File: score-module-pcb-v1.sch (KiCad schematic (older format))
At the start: 2 parts, among them P1 PINBALL-CONNECTOR, P2 PINBALL-CONNECTOR

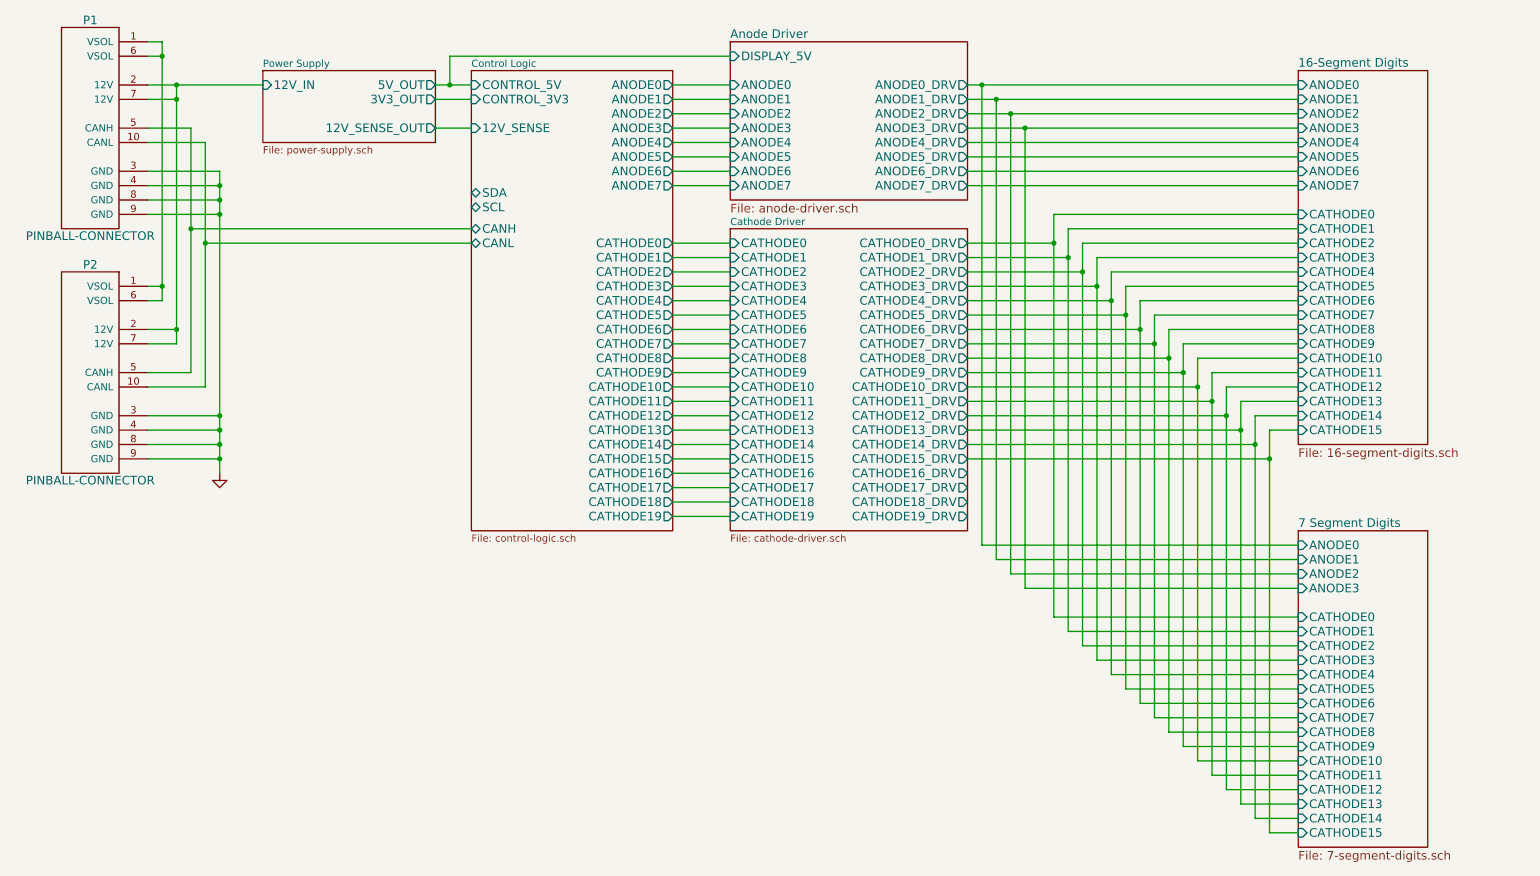
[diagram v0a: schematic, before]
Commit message: I think the layout is finished now. I'll check again after I sleep.
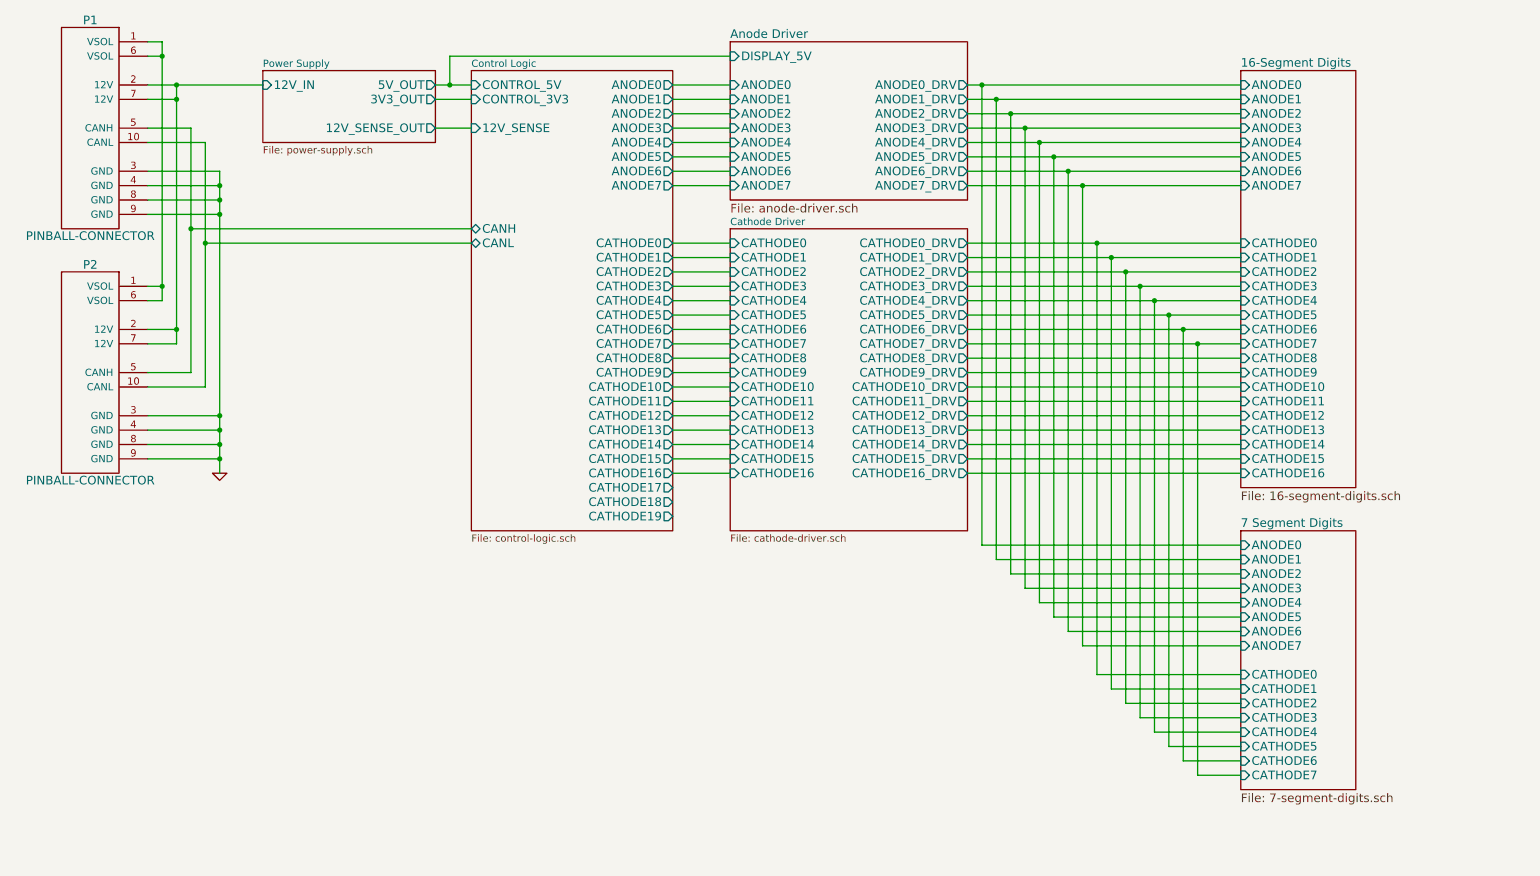
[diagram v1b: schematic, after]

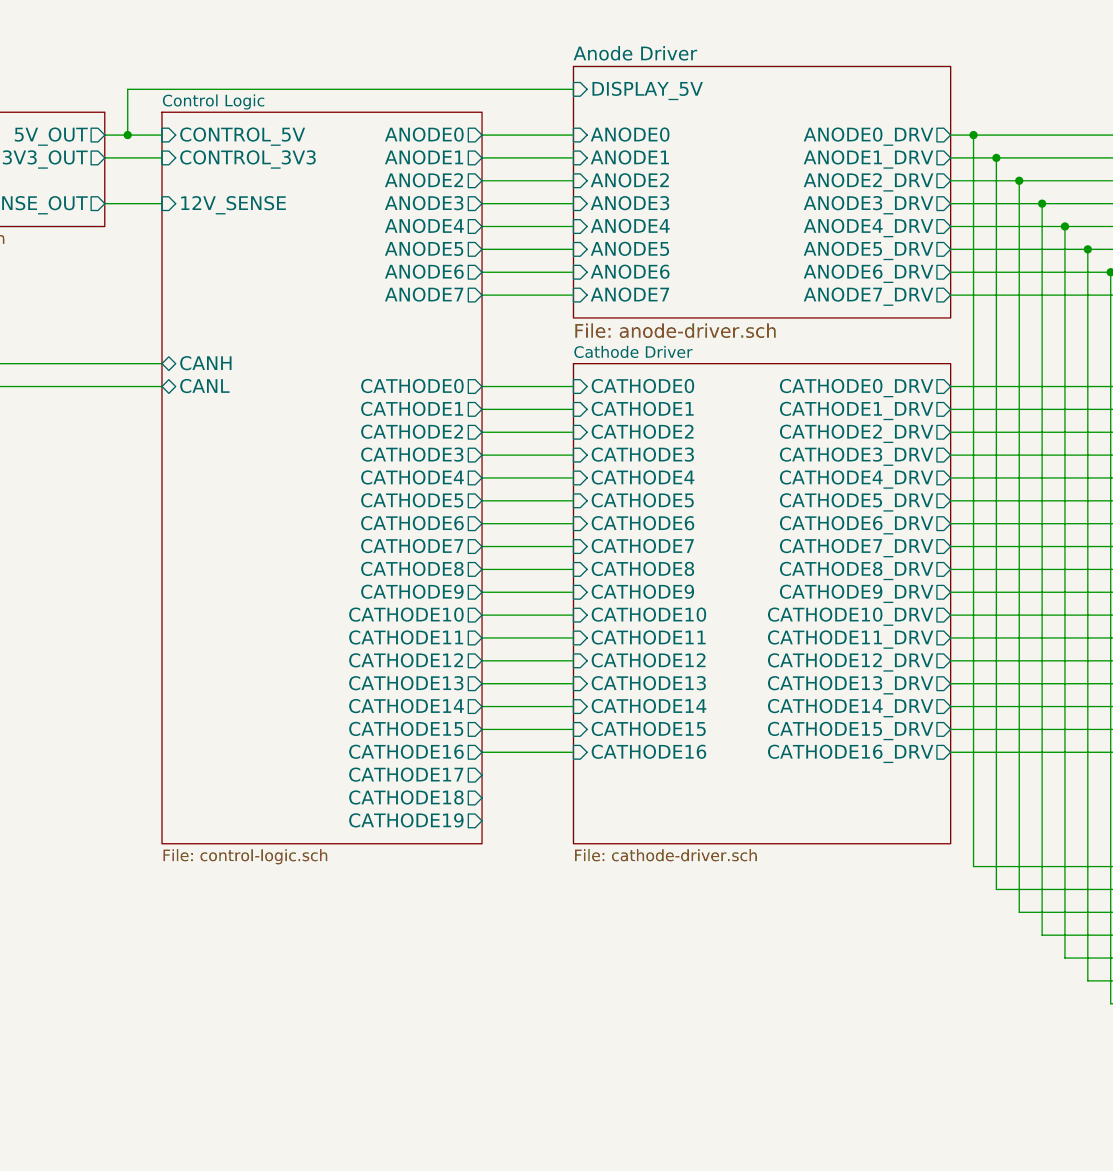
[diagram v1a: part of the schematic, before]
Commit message: Adding RGB LED driver
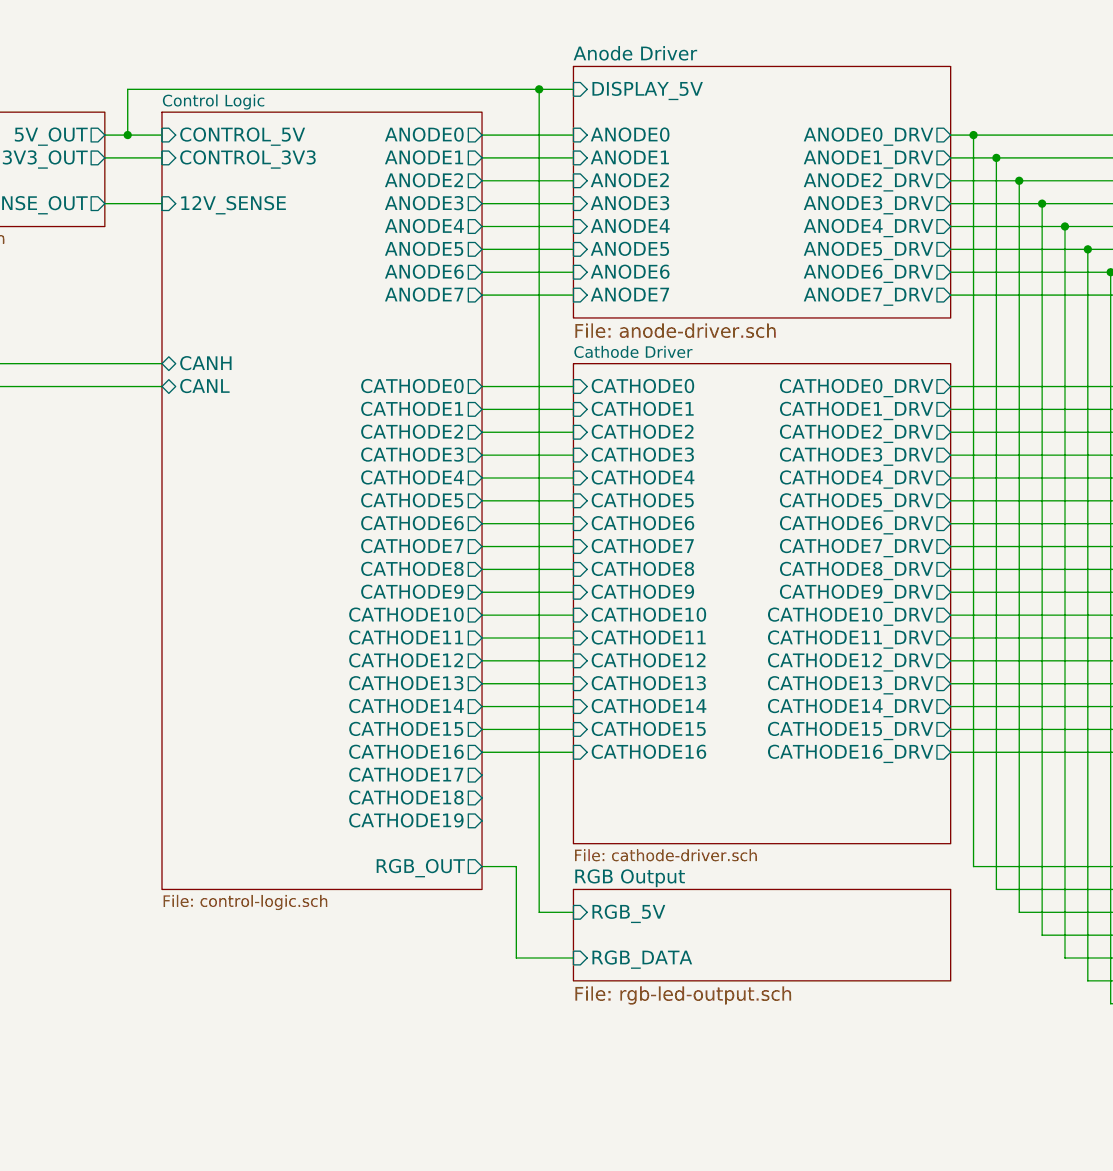
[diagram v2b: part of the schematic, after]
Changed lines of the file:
@@
 $Descr USLetter 11000 8500
 encoding utf-8
-Sheet 1 7
+Sheet 1 8
 Title "DIYPinball Score Display Module"
 Date "Tuesday, August 04, 2015"
@@
 $EndDescr
 $Sheet
-S 3650 900  1400 3200
+S 3650 900  1400 3400
 U 5323E468
 F0 "Control Logic" 50
@@
 F33 "ANODE7" O R 5050 1700 60
 F34 "ANODE3" O R 5050 1300 60
+F35 "RGB_OUT" O R 5050 4200 60
 $EndSheet
 $Comp
@@
 Wire Wire Line
 	7100 3700 9000 3700
+$Sheet
+S 5450 4300 1650 400
+U 5629DD81
+F0 "RGB Output" 60
+F1 "rgb-led-output.sch" 60
+F2 "RGB_DATA" I L 5450 4600 60
+F3 "RGB_5V" I L 5450 4400 60
+$EndSheet
+Wire Wire Line
+	5050 4200 5200 4200
+Wire Wire Line
+	5200 4200 5200 4600
+Wire Wire Line
+	5200 4600 5450 4600
+Wire Wire Line
+	5450 4400 5300 4400
+Wire Wire Line
+	5300 4400 5300 800
+Connection ~ 5300 800
 $EndSCHEMATC
